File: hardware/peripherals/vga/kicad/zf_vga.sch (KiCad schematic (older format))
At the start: 28 parts

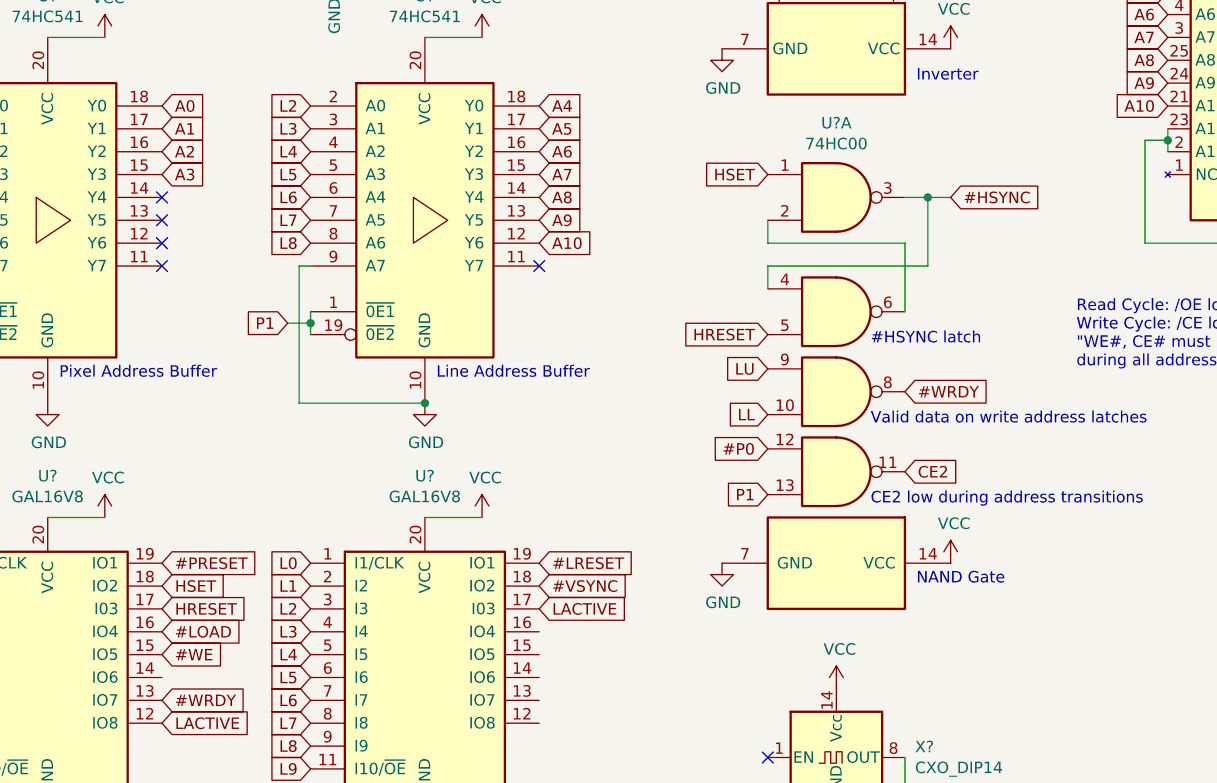
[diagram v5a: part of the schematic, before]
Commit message: #HSYNC SR latch
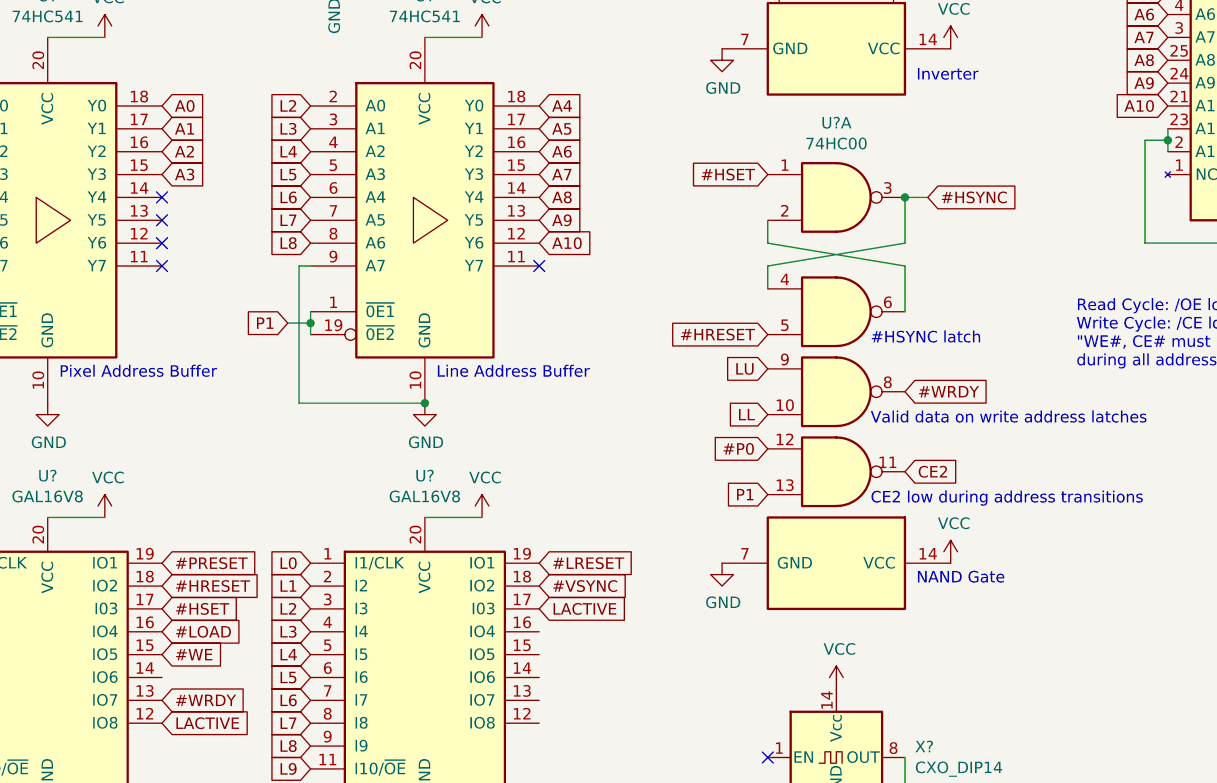
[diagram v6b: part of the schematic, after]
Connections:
- net HRESET renamed #HRESET
- net #HRESET: now also U?.18 (IO2); no longer U?.17 (I03)
- net HSET renamed #HSET
- net #HSET: now also U?.17 (I03); no longer U?.18 (IO2)
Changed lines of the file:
@@
 Text GLabel 2600 7200 0    50   Input ~ 0
 L9
-Text GLabel 1950 6400 2    50   Input ~ 0
-HSET
+Text GLabel 1950 6500 2    50   Input ~ 0
+#HSET
 Text GLabel 1950 6600 2    50   Input ~ 0
 #LOAD
@@
 NoConn ~ 10700 4150
 NoConn ~ 10700 4250
-$Comp
-L 74xx:74HC00 U?
-U 1 1 6222CFFF
-P 4900 4700
-F 0 "U?" H 4900 5025 50  0000 C CNN
-F 1 "74HC00" H 4900 4934 50  0000 C CNN
-F 2 "" H 4900 4700 50  0001 C CNN
-F 3 "http://www.ti.com/lit/gpn/sn74hc00" H 4900 4700 50  0001 C CNN
-	1    4900 4700
-	1    0    0    -1
-$EndComp
-Wire Wire Line
-	4600 5000 4600 5100
-Wire Wire Line
-	4600 4800 4600 4900
-Wire Wire Line
-	4600 4900 5200 4900
-Wire Wire Line
-	5200 4900 5200 5200
-Wire Wire Line
-	5300 5000 4600 5000
-Wire Wire Line
-	5200 4700 5300 4700
-Wire Wire Line
-	5300 4700 5300 5000
 Text GLabel 4600 4600 0    50   Input ~ 0
-HSET
+#HSET
 Text GLabel 4600 5300 0    50   Input ~ 0
-HRESET
+#HRESET
 Text GLabel 1950 7000 2    50   Input ~ 0
 LACTIVE
@@
 	1    0    0    -1
 $EndComp
-Text GLabel 1950 6500 2    50   Input ~ 0
-HRESET
-Wire Wire Line
-	5400 4700 5300 4700
-Connection ~ 5300 4700
+Text GLabel 1950 6400 2    50   Input ~ 0
+#HRESET
 Text GLabel 1950 6900 2    50   Input ~ 0
 #WRDY
@@
 Text GLabel 5200 5550 2    50   Input ~ 0
 #WRDY
-Text GLabel 5400 4700 2    50   Input ~ 0
+Text GLabel 5300 4700 2    50   Input ~ 0
 #HSYNC
 Text GLabel 4350 1100 0    50   Input ~ 0
@@
 Text GLabel 4350 2100 0    50   Input ~ 0
 P0
-Text Notes 5050 5350 0    50   ~ 0
-#HSYNC latch
 Text GLabel 4350 1600 0    50   Input ~ 0
 P1
@@
 NoConn ~ 9950 2300
 NoConn ~ 9950 2400
+$Comp
+L 74xx:74HC00 U?
+U 1 1 6222CFFF
+P 4900 4700
+F 0 "U?" H 4900 5025 50  0000 C CNN
+F 1 "74HC00" H 4900 4934 50  0000 C CNN
+F 2 "" H 4900 4700 50  0001 C CNN
+F 3 "http://www.ti.com/lit/gpn/sn74hc00" H 4900 4700 50  0001 C CNN
+	1    4900 4700
+	1    0    0    -1
+$EndComp
+Wire Wire Line
+	5200 4900 5200 4700
+Wire Wire Line
+	5200 5000 5200 5200
+Wire Wire Line
+	4600 5000 5200 4900
+Wire Wire Line
+	4600 5000 4600 5100
+Wire Wire Line
+	4600 4900 5200 5000
+Wire Wire Line
+	4600 4800 4600 4900
+Text Notes 5050 5350 0    50   ~ 0
+#HSYNC latch
+Wire Wire Line
+	5300 4700 5200 4700
+Connection ~ 5200 4700
 $EndSCHEMATC

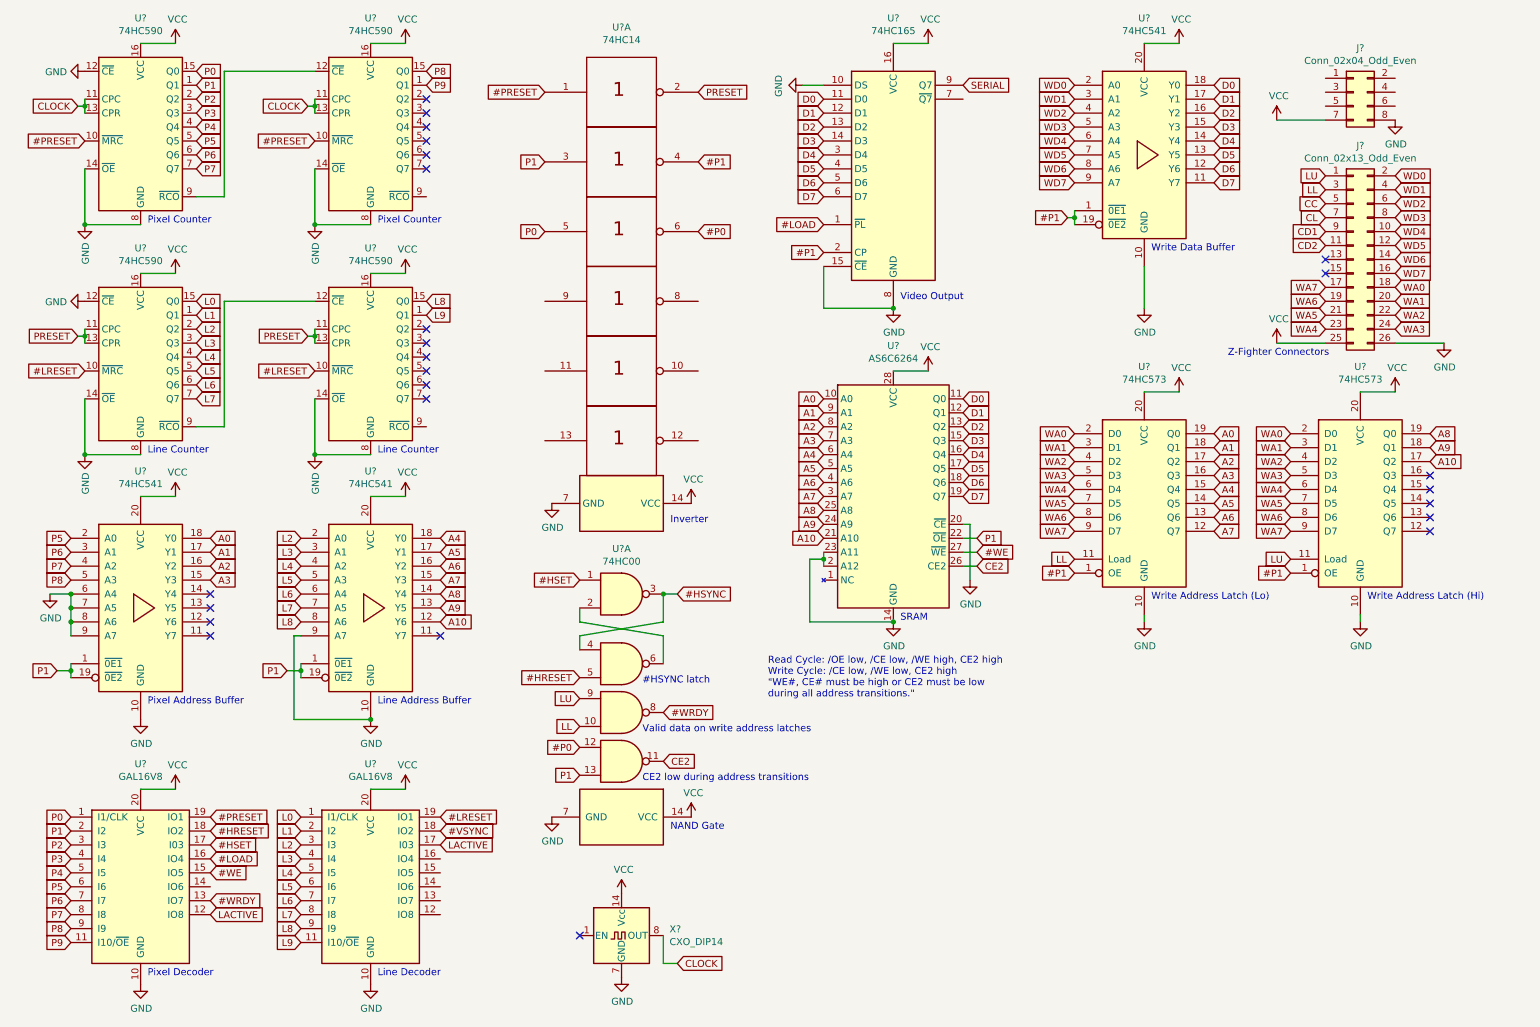
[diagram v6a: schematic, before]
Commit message: Added another NAND gate
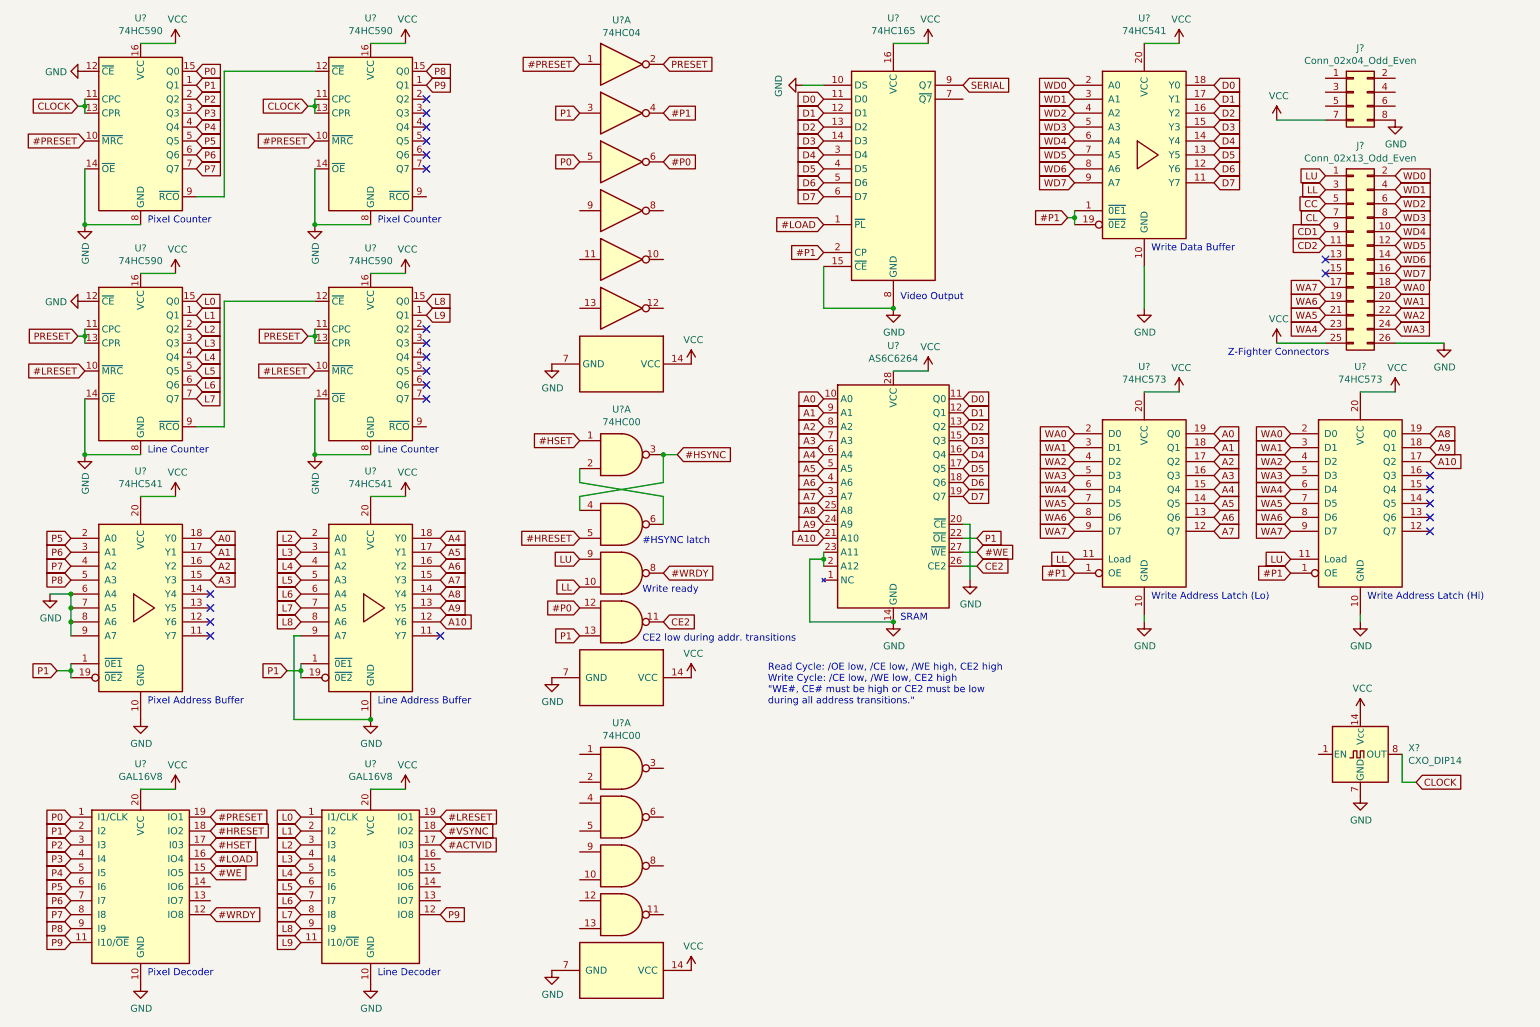
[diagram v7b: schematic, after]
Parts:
- removed U?: 74HC14, symbol 74xx_IEEE:7404
- removed U? (x5): 7404, symbol 74xx_IEEE:7404
- removed U?: 74HC04, symbol 74xx:74HC04
- added U? (x7): 74HC04, symbol 74xx:74HC04
- added U? (x5): 74HC00, symbol 74xx:74HC00
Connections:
- net #P0: now also U?.6
- net #P1: now also U?.4
- net #PRESET: now also U?.1
- net #WRDY: now also U?.12 (IO8); no longer U?.13 (IO7)
- net GND: now also U?.7 (GND), U?.7 (GND)
- net P0: now also U?.5
- net P1: now also U?.3
- net P9: now also U?.12 (IO8)
- net PRESET: now also U?.2
- net VCC: now also U?.14 (VCC), U?.14 (VCC)
- net LACTIVE renamed #ACTVID
- net #ACTVID: no longer U?.12 (IO8)
- no-connect marks 25 -> 24
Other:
- note added: "CE2 low during addr. transitions"
- note added: "Write ready"
- note removed: "CE2 low during address transitions"
- note removed: "Inverter"
- note removed: "NAND Gate"
- note removed: "Valid data on write address latches"
- moved on the sheet: U?A, X?

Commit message: #LOAD pulse monostable circuit
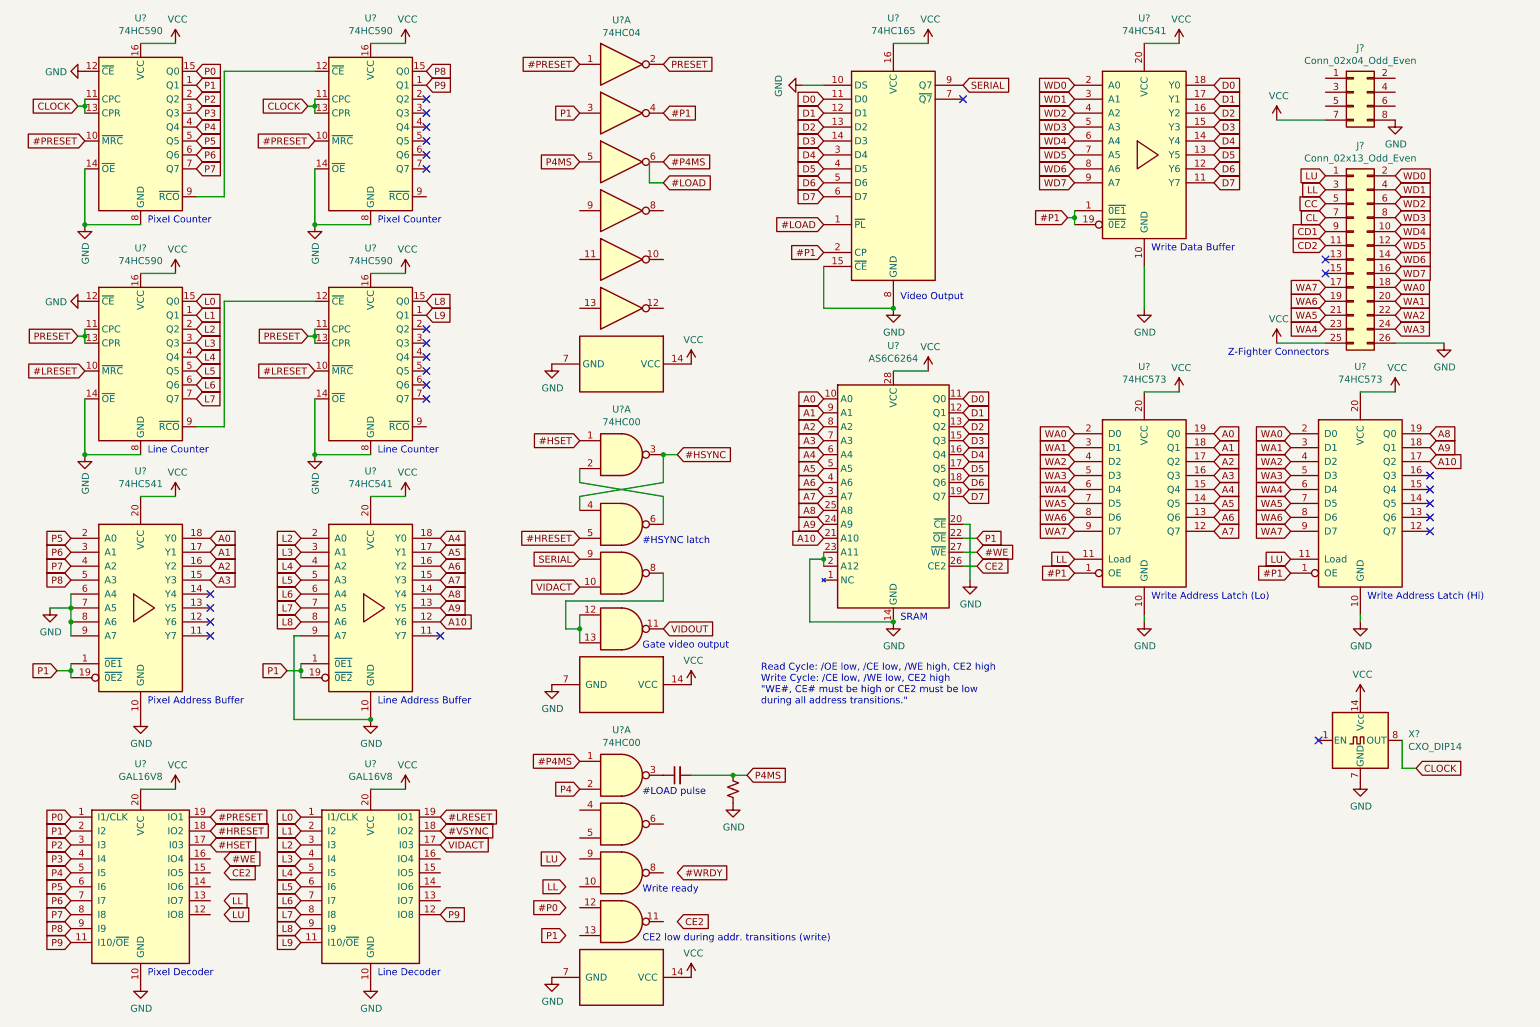
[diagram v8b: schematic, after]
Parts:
- added C?: C_Small, symbol Device:C_Small
- added R?: R_Small_US, symbol Device:R_Small_US
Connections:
- net #LOAD: no longer U?.16 (IO4)
- net #P0: no longer U?.12, U?.6
- net #WE: no longer U?.15 (IO5)
- net #WRDY: no longer U?.12 (IO8), U?.8
- net CE2: no longer U?.11
- net GND: now also R?.1
- net LL: no longer U?.10
- net LU: no longer U?.9
- net P0: no longer U?.5
- net P1: no longer U?.13
- net P4: now also U?.2
- net SERIAL: now also U?.9
- net #P4MS: now reaches U?.1
- net #P4MS: now also U?.6
- net at U?.3: now also C?.1
- net #ACTVID renamed VIDACT
- net VIDACT: now also U?.10
- new net: U?.12, U?.13, U?.8
- new net P4MS: C?.2, R?.2, U?.5
- new net VIDOUT: U?.11
- no-connect marks 24 -> 26
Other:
- note added: "#LOAD pulse"
- note added: "CE2 low during addr. transitions (write)"
- note added: "Gate video output"
- note removed: "CE2 low during addr. transitions"
- moved on the sheet: U?A, X?
